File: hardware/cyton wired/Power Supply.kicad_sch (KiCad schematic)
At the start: 2 parts

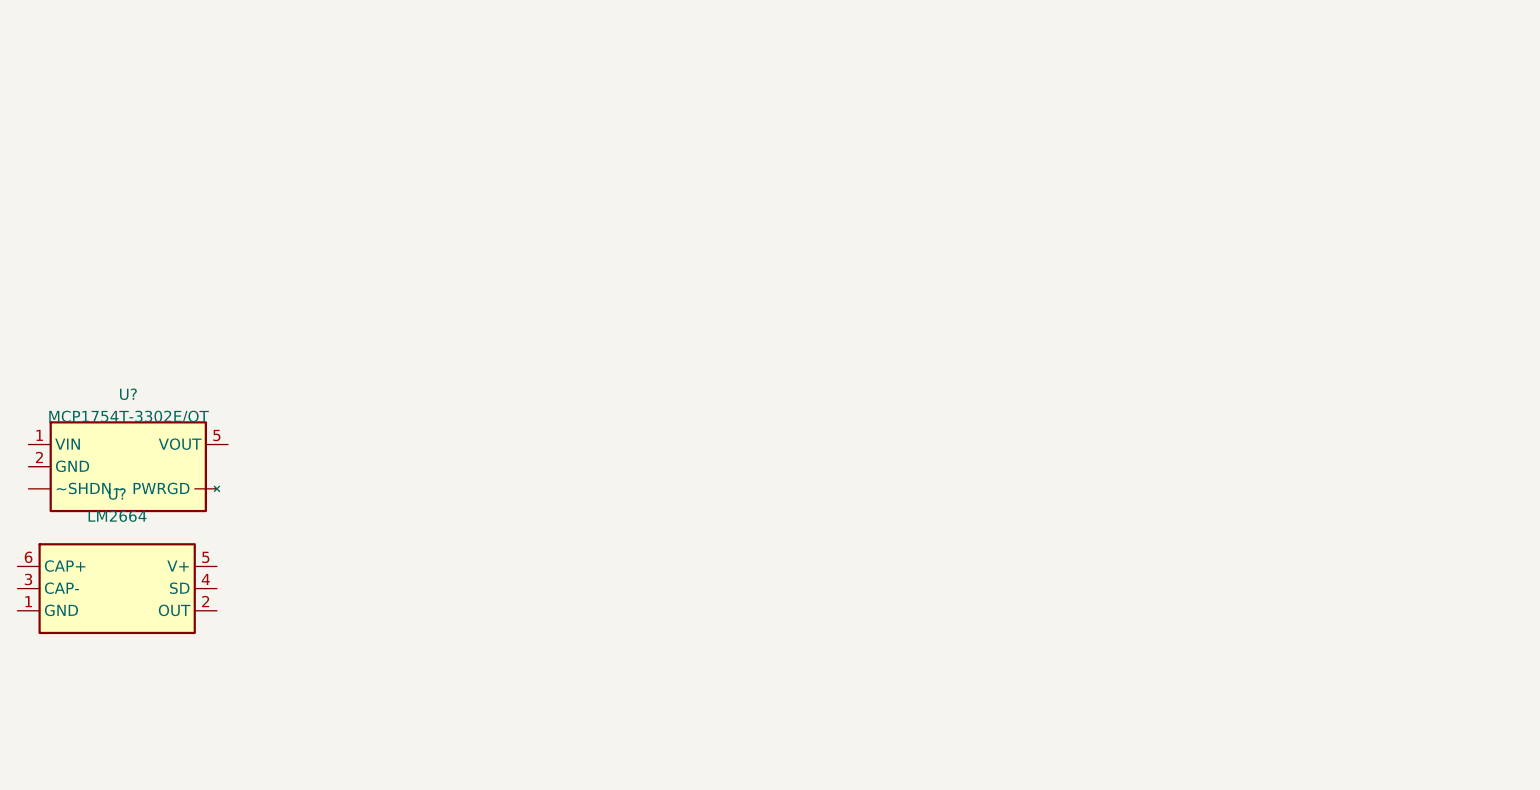
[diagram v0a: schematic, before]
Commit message: added power supply
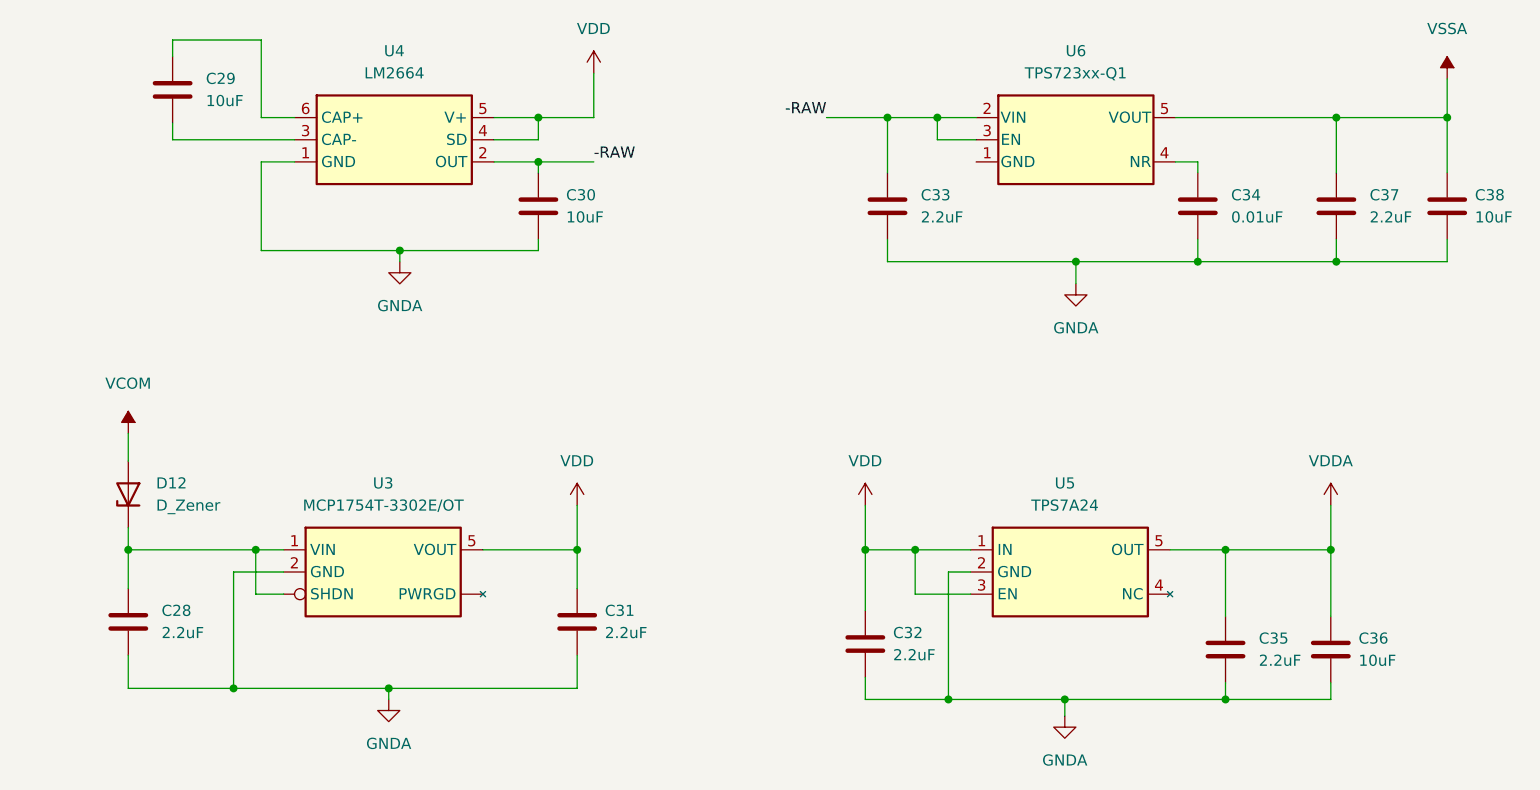
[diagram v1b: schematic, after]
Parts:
- removed U?: MCP1754T-3302E/OT, Package_TO_SOT_SMD:SOT-23-5, symbol Brain-4ce_Regulator_Linear:MCP1754T-3302E/OT
- removed U?: LM2664, Package_TO_SOT_SMD:SOT-23-6, symbol Brain-4ce_Regulator_SwitchedCapacitor:LM2664
- added C28, C31, C32, C33, C35, C37: 2.2uF, Capacitor_SMD:C_0402_1005Metric, symbol Device:C
- added C29, C30, C36, C38: 10uF, Capacitor_SMD:C_0603_1608Metric, symbol Device:C
- added C34: 0.01uF, Capacitor_SMD:C_0402_1005Metric, symbol Device:C
- added D12: D_Zener, Diode_SMD:D_SOD-323, symbol Device:D_Zener
- added U3: MCP1754T-3302E/OT, Package_TO_SOT_SMD:SOT-23-5, symbol Brain-4ce_Regulator_Linear:MCP1754T-3302E/OT
- added U4: LM2664, Package_TO_SOT_SMD:SOT-23-6, symbol Brain-4ce_Regulator_SwitchedCapacitor:LM2664
- added U5: TPS7A24, Package_TO_SOT_SMD:SOT-23-5, symbol Brain-4ce_Regulator_Linear:TPS7A24
- added U6: TPS723xx-Q1, Package_TO_SOT_SMD:SOT-23-5, symbol Brain-4ce_Regulator_Linear:TPS723xx-Q1
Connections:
- new net: C28.1, D12.1 (K), U3. (SHDN), U3.1 (VIN)
- new net: C29.2, U4.3 (CAP-)
- new net: C29.1, U4.6 (CAP+)
- new net: C34.1, U6.4 (NR)
- new net -RAW: C30.1, C33.1, U4.2 (OUT), U6.2 (VIN), U6.3 (EN)
- new net GNDA: C28.2, C30.2, C31.2, C32.2, C33.2, C34.2, C35.2, C36.2, C37.2, C38.2, U3.2 (GND), U4.1 (GND), U5.2 (GND)
- new net VCOM: D12.2 (A)
- new net VDD: C31.1, C32.1, U3.5 (VOUT), U4.4 (SD), U4.5 (V+), U5.1 (IN), U5.3 (EN)
- new net VDDA: C35.1, C36.1, U5.5 (OUT)
- new net VSSA: C37.1, C38.1, U6.5 (VOUT)

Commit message: added power supply
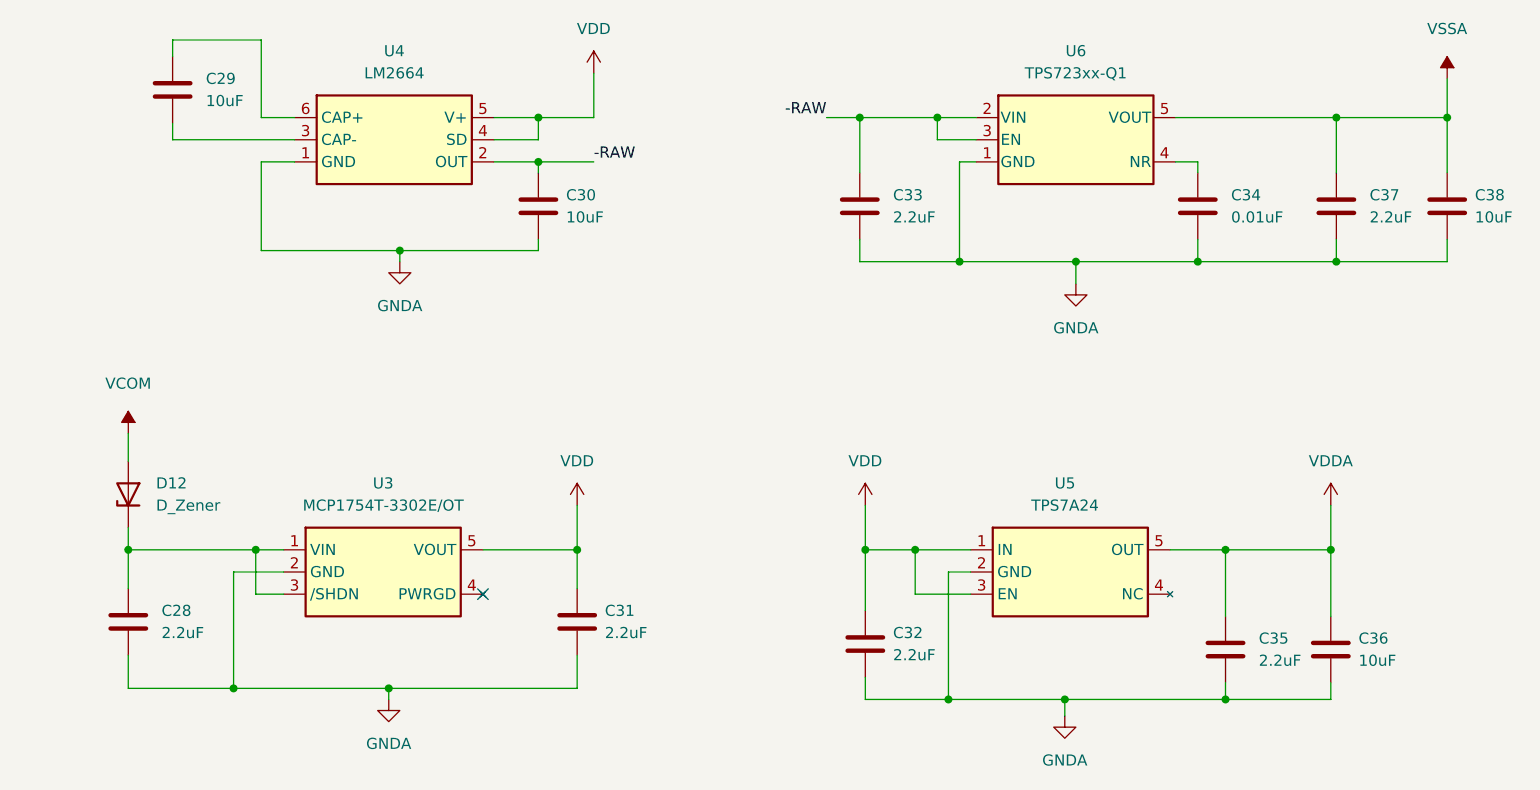
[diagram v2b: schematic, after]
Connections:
- net GNDA: now also U6.1 (GND)
- net at C28.1, D12.1 (K), U3.1 (VIN): now also U3.3 (/SHDN); no longer U3. (SHDN)
- no-connect marks 0 -> 1
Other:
- moved on the sheet: C33
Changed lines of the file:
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@@
   (junction (at 193.675 116.205) (diameter 0) (color 0 0 0 0)
   )
+  (junction (at 181.61 66.04) (diameter 0) (color 0 0 0 0)
+  )
   (junction (at 237.49 49.53) (diameter 0) (color 0 0 0 0)
   )
-  (junction (at 173.355 49.53) (diameter 0) (color 0 0 0 0)
+  (junction (at 170.18 49.53) (diameter 0) (color 0 0 0 0)
   )
   (junction (at 98.425 114.935) (diameter 0) (color 0 0 0 0)
@@
   (junction (at 100.965 99.06) (diameter 0) (color 0 0 0 0)
   )
+  (no_connect (at 127 104.14))
   (wire (pts (xy 176.53 99.06) (xy 170.815 99.06))
     (stroke (width 0) (type default) (color 0 0 0 0))
@@
     (stroke (width 0) (type default) (color 0 0 0 0))
   )
-  (wire (pts (xy 173.355 63.5) (xy 173.355 66.04))
+  (wire (pts (xy 170.18 63.5) (xy 170.18 66.04))
     (stroke (width 0) (type default) (color 0 0 0 0))
   )
@@
     (stroke (width 0) (type default) (color 0 0 0 0))
   )
+  (wire (pts (xy 183.515 54.61) (xy 181.61 54.61))
+    (stroke (width 0) (type default) (color 0 0 0 0))
+  )
   (wire (pts (xy 133.35 52.07) (xy 133.35 49.53))
     (stroke (width 0) (type default) (color 0 0 0 0))
@@
     (stroke (width 0) (type default) (color 0 0 0 0))
   )
-  (wire (pts (xy 173.355 66.04) (xy 194.945 66.04))
-    (stroke (width 0) (type default) (color 0 0 0 0))
-  )
-  (wire (pts (xy 173.355 49.53) (xy 173.355 55.88))
+  (wire (pts (xy 170.18 66.04) (xy 181.61 66.04))
+    (stroke (width 0) (type default) (color 0 0 0 0))
+  )
+  (wire (pts (xy 170.18 49.53) (xy 170.18 55.88))
     (stroke (width 0) (type default) (color 0 0 0 0))
   )
@@
     (stroke (width 0) (type default) (color 0 0 0 0))
   )
-  (wire (pts (xy 179.07 49.53) (xy 173.355 49.53))
+  (wire (pts (xy 170.18 49.53) (xy 179.07 49.53))
     (stroke (width 0) (type default) (color 0 0 0 0))
   )
@@
     (stroke (width 0) (type default) (color 0 0 0 0))
   )
+  (wire (pts (xy 181.61 66.04) (xy 194.945 66.04))
+    (stroke (width 0) (type default) (color 0 0 0 0))
+  )
   (wire (pts (xy 91.44 40.64) (xy 91.44 42.545))
     (stroke (width 0) (type default) (color 0 0 0 0))
@@
     (stroke (width 0) (type default) (color 0 0 0 0))
   )
-  (wire (pts (xy 166.37 49.53) (xy 173.355 49.53))
+  (wire (pts (xy 181.61 54.61) (xy 181.61 66.04))
+    (stroke (width 0) (type default) (color 0 0 0 0))
+  )
+  (wire (pts (xy 166.37 49.53) (xy 170.18 49.53))
     (stroke (width 0) (type default) (color 0 0 0 0))
   )
@@
       (effects (font (size 1.27 1.27)) hide)
     )
-    (pin "")
-    (pin "")
-    (pin "1")
-    (pin "2")
+    (pin "1")
+    (pin "2")
+    (pin "3")
+    (pin "4")
     (pin "5")
   )
@@
     (pin "2")
   )
-  (symbol (lib_id "Device:C") (at 173.355 59.69 0) (unit 1)
-    (in_bom yes) (on_board yes) (fields_autoplaced)
-    (property "Reference" "C33" (id 0) (at 177.165 58.4199 0)
-      (effects (font (size 1.27 1.27)) (justify left))
-    )
-    (property "Value" "2.2uF" (id 1) (at 177.165 60.9599 0)
-      (effects (font (size 1.27 1.27)) (justify left))
-    )
-    (property "Footprint" "Capacitor_SMD:C_0402_1005Metric" (id 2) (at 174.3202 63.5 0)
-      (effects (font (size 1.27 1.27)) hide)
-    )
-    (property "Datasheet" "~" (id 3) (at 173.355 59.69 0)
-      (effects (font (size 1.27 1.27)) hide)
-    )
+  (symbol (lib_id "Device:C") (at 170.18 59.69 0) (unit 1)
+    (in_bom yes) (on_board yes) (fields_autoplaced)
+    (property "Reference" "C33" (id 0) (at 173.99 58.4199 0)
+      (effects (font (size 1.27 1.27)) (justify left))
+    )
+    (property "Value" "2.2uF" (id 1) (at 173.99 60.9599 0)
+      (effects (font (size 1.27 1.27)) (justify left))
+    )
+    (property "Footprint" "Capacitor_SMD:C_0402_1005Metric" (id 2) (at 171.1452 63.5 0)
+      (effects (font (size 1.27 1.27)) hide)
+    )
+    (property "Datasheet" "~" (id 3) (at 170.18 59.69 0)
+      (effects (font (size 1.27 1.27)) hide)
+    )
